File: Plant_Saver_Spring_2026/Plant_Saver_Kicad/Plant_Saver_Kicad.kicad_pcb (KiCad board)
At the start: 2 copper layers, 106 parts, among them J10 DM3D-SF, J2 SBH11-PBPC-D05-ST-BK, J3 SM04B-SRSS-TB, J5 Conn_01x02_Pin, J6 Conn_01x06_Socket, J7 S3B-PH-K-S, J8 54-00284, J9 1.25mm, Q1 G09P02L, Q10 G09P02L, Q11 ISP12DP06NMXTSA1, Q12 G09P02L, Q2 G09P02L, Q3 ISP12DP06NMXTSA1, Q4 G09P02L, Q5 G09P02L, Q6 G09P02L, Q7 G09P02L, Q8 G09P02L, Q9 G09P02L, SW1 Reset, SW2 25336NA, SW3 Boot, SW4 SA72SB0, U1 CDBA140SL-HF, U10 DW03C, U11 CDBA140SL-HF, U12 LP38511TJ-ADJ/NOPB, U13 MCP73833-xxx-UN, U14 MCP6234, U15 MCP73833-xxx-UN, U16 MCP6547T_I_MS, U2 CDBA140SL-HF, U3 CDBA140SL-HF, U4 CDBA140SL-HF, U5 ESP32-WROOM-32E-N16, U9 CDBA140SL-HF

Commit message: Rough PCB Layout
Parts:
- moved TP4 141.7 mm to (244.5, 48.3)
- moved TP3 138.9 mm to (244.6, 53.5)
- moved J8 133.5 mm to (50.8, 133.3), turned to -90 degrees
- moved TP7 131.6 mm to (60.9, 134.3)
- moved R6 123.8 mm to (55.3, 139.1)
- moved R5 123.1 mm to (55.7, 128.7)
- moved J6 117.8 mm to (225.9, 92.9)
- moved TP5 115.6 mm to (230.9, 103.2)
- moved TP6 115.4 mm to (230.9, 100.0)
- moved C13 114.3 mm to (80.6, 133.0)
- moved C14 114.3 mm to (87.4, 137.1)
- moved R36 114.3 mm to (80.0, 128.9)
- moved U15 114.3 mm to (82.1, 137.3)
- moved SC1 111.1 mm to (39.7, 99.8)
- moved SC2 111.1 mm to (39.7, 103.9)
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
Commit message: Refined PCB layout
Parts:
- removed R12: 200K, Resistor_THT:R_Axial_DIN0207_L6.3mm_D2.5mm_P10.16mm_Horizontal
- added C15: 0.1uF, Capacitor_SMD:C_1206_3216Metric_Pad1.33x1.80mm_HandSolder, F.Cu at (84.1, 100.0)
- added C16: 0.1uF, Capacitor_SMD:C_1206_3216Metric_Pad1.33x1.80mm_HandSolder, F.Cu at (137.5, 77.5)
- added R44: 10K, Resistor_SMD:R_1206_3216Metric_Pad1.30x1.75mm_HandSolder, F.Cu at (265.9, 136.8)
- added R45: 10K, Resistor_SMD:R_1206_3216Metric_Pad1.30x1.75mm_HandSolder, F.Cu at (265.9, 140.1)
- C1, C2, C3, C4, C6, C7: footprint Capacitor_THT:C_Disc_D4.7mm_W2.5mm_P5.00mm -> Capacitor_SMD:C_1206_3216Metric_Pad1.33x1.80mm_HandSolder
- C11, C12, C13, C5: footprint C410C105K5R5TA7200:CAP_C410C_AX_X7R_AXIMAX_KEM -> Capacitor_SMD:C_1206_3216Metric_Pad1.33x1.80mm_HandSolder
- C14, C8: footprint Capacitor_THT:C_Disc_D3.8mm_W2.6mm_P2.50mm -> Capacitor_SMD:C_1206_3216Metric_Pad1.33x1.80mm_HandSolder
- R1, R11, R13, R14, R15, R2, R3, R4, R42, R43, R5, R6, R7, R8: footprint Resistor_THT:R_Axial_DIN0207_L6.3mm_D2.5mm_P10.16mm_Horizontal -> Resistor_SMD:R_1206_3216Metric_Pad1.30x1.75mm_HandSolder
- moved R21 149.5 mm to (80.5, 143.5), turned to -90 degrees
- moved R22 146.4 mm to (83.5, 143.5), turned to -90 degrees
- moved R23 143.5 mm to (86.5, 143.5), turned to -90 degrees
- moved R18 141.0 mm to (89.5, 143.6), turned to -90 degrees
- moved R19 137.7 mm to (92.5, 143.6), turned to -90 degrees
- moved R20 134.6 mm to (95.5, 143.6), turned to -90 degrees
- moved C9 130.2 mm to (94.5, 155.5), turned to 90 degrees
- moved C10 130.0 mm to (94.5, 150.0), turned to -90 degrees
- moved J10 125.9 mm to (86.0, 148.3)
- moved R11 92.4 mm to (192.4, 88.8)
- moved R4 89.0 mm to (165.6, 140.0)
- moved R43 84.6 mm to (148.4, 95.0), turned to 180 degrees
- moved U6 80.4 mm to (265.7, 131.4)
- moved TP4 80.4 mm to (272.2, 123.8)
- moved J2 80.4 mm to (208.8, 128.0)
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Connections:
- J10 pad 2: Vperiph -> uSD_CS
- R22 pad 2: Vperiph -> uSD_CS
- R32 pad 1: Net-(U14E-V-) -> GND
- R33 pad 1: Net-(U14E-V-) -> GND
- R34 pad 1: Net-(U14E-V-) -> GND
- R35 pad 1: Net-(U14E-V-) -> GND
- U14 pad 1: Net-(U14A--) -> V_Solar1
- U14 pad 11: Net-(U14E-V-) -> GND
- U14 pad 2: Net-(U14A--) -> V_Solar1
- U16 pad 8: Vbus -> Net-(U16C-V+)
- U5 pad 29: Vperiph -> uSD_CS

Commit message: Began PCB routing
Routed solar input, measurement and protections
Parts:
- moved J2 183.1 mm to (28.1, 157.0)
- moved J3 183.1 mm to (55.5, 159.0)
- moved J7 183.1 mm to (69.5, 155.7)
- moved R44 183.1 mm to (85.2, 165.8)
- moved R45 183.1 mm to (85.2, 169.1)
- moved TP3 183.1 mm to (91.6, 158.0)
- moved U6 183.1 mm to (85.0, 160.4)
- moved TP4 183.1 mm to (91.4, 152.8)
- moved J8 156.9 mm to (189.0, 74.0), turned to 90 degrees
- moved TP7 154.1 mm to (191.4, 65.0), turned to -90 degrees
- moved SW2 153.8 mm to (187.9, 117.0), turned to 90 degrees
- moved R6 151.8 mm to (185.4, 64.0), turned to 180 degrees
- moved R5 148.5 mm to (185.4, 66.5), turned to 180 degrees
- moved U15 141.7 mm to (192.3, 84.3), turned to -90 degrees
- moved C13 140.1 mm to (186.9, 82.3), turned to 180 degrees
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- renumbered TP1 to GND, TP2 to SOL
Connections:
- U5 pad 38: unconnected-(U5-GND-Pad38) -> GND
- U5 pad 39: unconnected-(U5-GND-Pad39) -> GND
- U5 pad 40: unconnected-(U5-GND-Pad40) -> GND
- U5 pad 41: unconnected-(U5-GND-Pad41) -> GND
- U5 pad 42: unconnected-(U5-GND-Pad42) -> GND
- U5 pad 43: unconnected-(U5-GND-Pad43) -> GND
- U5 pad 44: unconnected-(U5-GND-Pad44) -> GND
- U5 pad 45: unconnected-(U5-GND-Pad45) -> GND
- U5 pad 46: unconnected-(U5-GND-Pad46) -> GND
- U5 pad 47: unconnected-(U5-GND-Pad47) -> GND
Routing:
- net /Power_And_Charging/Solar: track 0.00 -> 60.3 mm
- net GND: track 0.00 -> 58.7 mm
- net /Solar_Measurement_Dual/Vin1: track 0.00 -> 31.4 mm
- net /Solar_Measurement_Dual/Vin4: track 0.00 -> 25.9 mm
- net Net-(U16B--): track 0.00 -> 25.7 mm
- net /Solar_Measurement_Dual/Vin3: track 0.00 -> 23.4 mm
- net Net-(U16A-+): track 0.00 -> 23.2 mm
- net Net-(Q11-G): track 0.00 -> 21.6 mm
- net /Solar_Measurement_Dual/Vin2: track 0.00 -> 20.9 mm
- net Net-(Q11-D): track 0.00 -> 18.7 mm
- net Net-(U14A-+): track 0.00 -> 17.8 mm
- net Net-(U16A--): track 0.00 -> 16.9 mm
- net Net-(U14B-+): track 0.00 -> 15.5 mm
- net Vbus: track 0.00 -> 9.01 mm
- net /Power_And_Charging/UOVLO_Solar/Vout: track 0.00 -> 6.94 mm
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
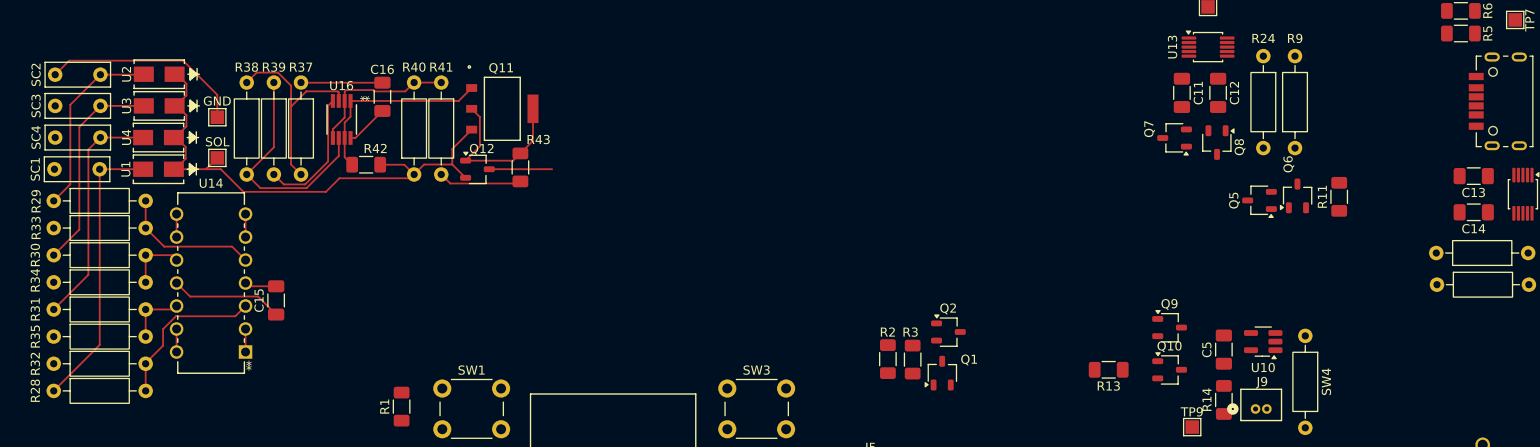
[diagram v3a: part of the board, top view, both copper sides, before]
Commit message: Re-routed to fix issue on schematic
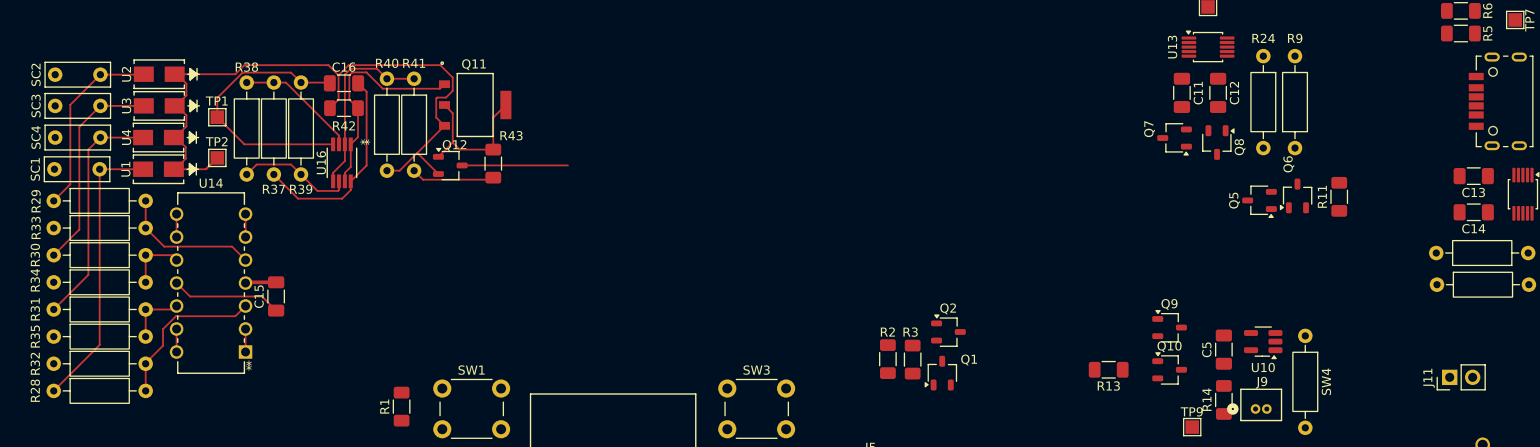
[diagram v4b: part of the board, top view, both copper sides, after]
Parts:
- added J11: Test, Connector_PinHeader_2.54mm:PinHeader_1x02_P2.54mm_Vertical, F.Cu at (184.2, 104.5)
- moved R37 10.6 mm to (54.2, 82.1), turned to 90 degrees
- moved R39 10.6 mm to (57.2, 82.1), turned to 90 degrees
- moved R42 6.71 mm to (62.0, 74.8), turned to 0 degrees
- moved U16 4.79 mm to (61.8, 80.8)
- moved C16 4.51 mm to (62.0, 72.0), turned to 180 degrees
- moved Q11 3.03 mm to (76.5, 74.4)
- moved Q12 3.03 mm to (73.8, 81.1)
- moved R40 3.03 mm to (66.8, 81.7)
- moved R41 3.03 mm to (69.8, 71.5)
- moved R43 3.03 mm to (78.5, 80.9)
- moved C15 0.44 mm to (54.5, 95.6)
- renumbered GND to TP1, SOL to TP2
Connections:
- C16 pad 2: Net-(U16C-V+) -> GND
- U16 pad 8: Net-(U16C-V+) -> Vbus
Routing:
- net /Power_And_Charging/Solar: track 60.3 -> 76.0 mm
- net Vbus: track 9.01 -> 22.9 mm
- net Net-(U16B--): track 25.7 -> 12.9 mm
- net Net-(U16A-+): track 23.2 -> 13.6 mm
- net GND: track 58.7 -> 51.8 mm
- net Net-(U16C-V+): track 4.76 -> 0.00 mm
- net /Power_And_Charging/UOVLO_Solar/Vout: track 6.94 -> 11.7 mm
- net Net-(U16A--): track 16.9 -> 20.8 mm
- net Net-(Q11-G): track 21.6 -> 24.3 mm
- net Net-(Q11-D): track 18.7 -> 17.1 mm
